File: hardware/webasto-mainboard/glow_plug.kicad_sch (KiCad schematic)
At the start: 23 parts, among them Q11 SSM3J374R, Q12 2N7002, Q13 SUD50P04-08, Q14 SUD50P04-08, Q15 SUD50P04-08, Q16 SUD50P04-08, Q17 SUD50P04-08, Q18 2N7002, Q19 2N7002, U6 LM7805_TO220, U7 INA219BxDCN

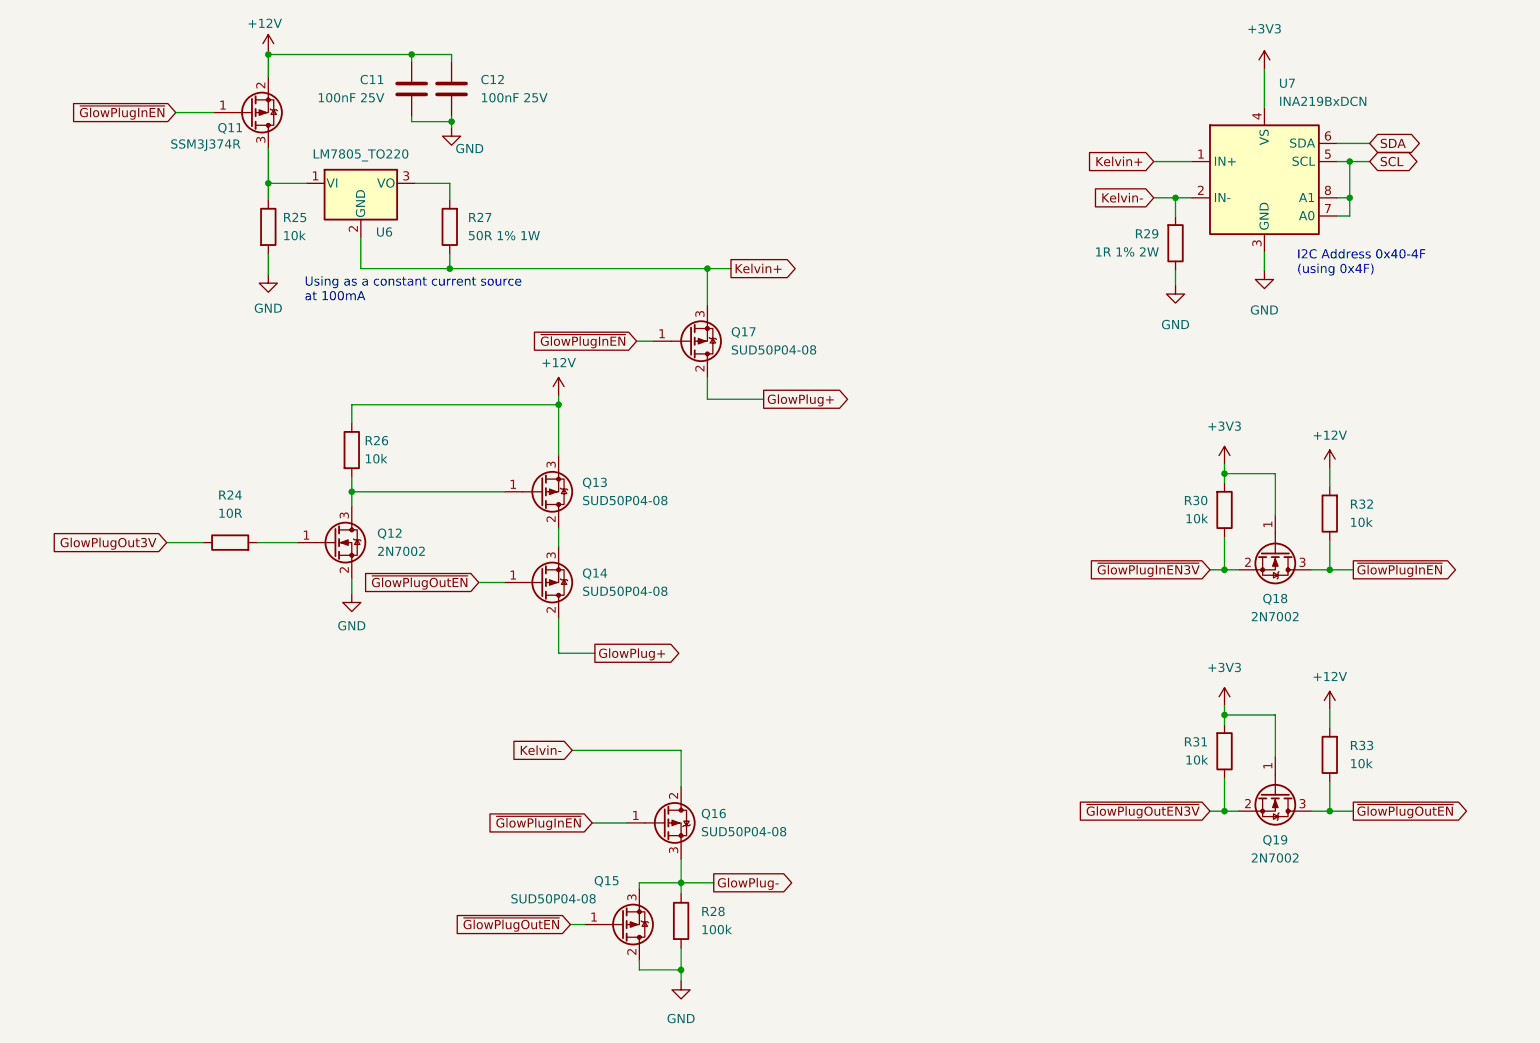
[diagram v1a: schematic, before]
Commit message: Added the LEDs onto the board and init
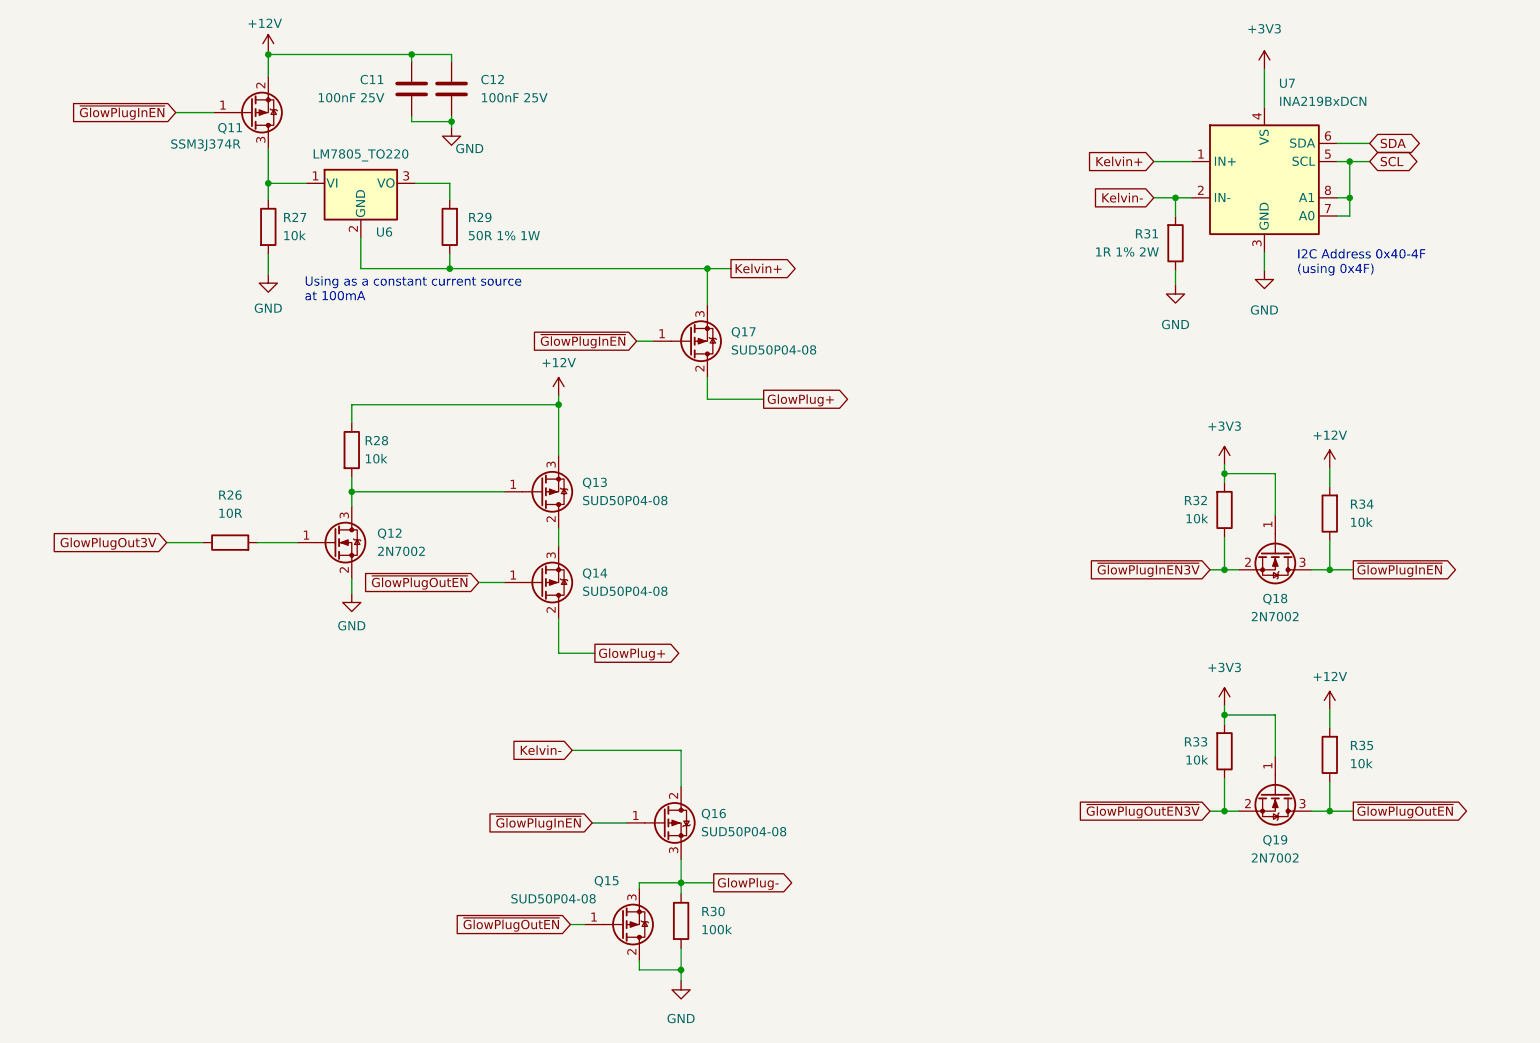
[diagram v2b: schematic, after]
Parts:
- renumbered R24 to R26, R25 to R27, R26 to R28, R27 to R29, R28 to R30, R29 to R31, R30 to R32, R31 to R33, R32 to R34, R33 to R35
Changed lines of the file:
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@@
   (symbol (lib_name "+3V3_1") (lib_id "power:+3V3") (at 202.565 29.972 0) (unit 1)
     (in_bom yes) (on_board yes) (fields_autoplaced)
-    (property "Reference" "#PWR063" (id 0) (at 202.565 33.782 0)
+    (property "Reference" "#PWR065" (id 0) (at 202.565 33.782 0)
       (effects (font (size 1.27 1.27)) hide)
     )
@@
   (symbol (lib_name "GND_8") (lib_id "power:GND") (at 202.565 58.166 0) (unit 1)
     (in_bom yes) (on_board yes) (fields_autoplaced)
-    (property "Reference" "#PWR064" (id 0) (at 202.565 64.516 0)
+    (property "Reference" "#PWR066" (id 0) (at 202.565 64.516 0)
       (effects (font (size 1.27 1.27)) hide)
     )
@@
   (symbol (lib_id "Device:R") (at 120.904 149.225 0) (unit 1)
     (in_bom yes) (on_board yes) (fields_autoplaced)
-    (property "Reference" "R28" (id 0) (at 123.698 147.9549 0)
+    (property "Reference" "R30" (id 0) (at 123.698 147.9549 0)
       (effects (font (size 1.27 1.27)) (justify left))
     )
@@
   (symbol (lib_id "Device:R") (at 74.803 83.312 0) (unit 1)
     (in_bom yes) (on_board yes) (fields_autoplaced)
-    (property "Reference" "R26" (id 0) (at 76.581 82.0419 0)
+    (property "Reference" "R28" (id 0) (at 76.581 82.0419 0)
       (effects (font (size 1.27 1.27)) (justify left))
     )
@@
   (symbol (lib_id "Device:R") (at 88.519 52.07 180) (unit 1)
     (in_bom yes) (on_board yes)
-    (property "Reference" "R27" (id 0) (at 91.059 50.7999 0)
+    (property "Reference" "R29" (id 0) (at 91.059 50.7999 0)
       (effects (font (size 1.27 1.27)) (justify right))
     )
@@
   (symbol (lib_name "+3V3_2") (lib_id "power:+3V3") (at 196.977 85.344 0) (unit 1)
     (in_bom yes) (on_board yes) (fields_autoplaced)
-    (property "Reference" "#PWR061" (id 0) (at 196.977 89.154 0)
+    (property "Reference" "#PWR063" (id 0) (at 196.977 89.154 0)
       (effects (font (size 1.27 1.27)) hide)
     )
@@
   (symbol (lib_name "GND_2") (lib_id "power:GND") (at 74.803 103.378 0) (unit 1)
     (in_bom yes) (on_board yes) (fields_autoplaced)
-    (property "Reference" "#PWR056" (id 0) (at 74.803 109.728 0)
+    (property "Reference" "#PWR058" (id 0) (at 74.803 109.728 0)
       (effects (font (size 1.27 1.27)) hide)
     )
@@
   (symbol (lib_id "Device:R") (at 63.119 52.07 0) (unit 1)
     (in_bom yes) (on_board yes)
-    (property "Reference" "R25" (id 0) (at 65.151 50.7999 0)
+    (property "Reference" "R27" (id 0) (at 65.151 50.7999 0)
       (effects (font (size 1.27 1.27)) (justify left))
     )
@@
   (symbol (lib_name "+3V3_2") (lib_id "power:+3V3") (at 196.977 119.126 0) (unit 1)
     (in_bom yes) (on_board yes) (fields_autoplaced)
-    (property "Reference" "#PWR062" (id 0) (at 196.977 122.936 0)
+    (property "Reference" "#PWR064" (id 0) (at 196.977 122.936 0)
       (effects (font (size 1.27 1.27)) hide)
     )
@@
   (symbol (lib_id "Device:R") (at 57.785 96.266 90) (unit 1)
     (in_bom yes) (on_board yes) (fields_autoplaced)
-    (property "Reference" "R24" (id 0) (at 57.785 89.662 90))
+    (property "Reference" "R26" (id 0) (at 57.785 89.662 90))
     (property "Value" "10R" (id 1) (at 57.785 92.202 90))
     (property "Footprint" "Resistor_SMD:R_0805_2012Metric_Pad1.20x1.40mm_HandSolder" (id 2) (at 57.785 98.044 90)
@@
   (symbol (lib_id "Device:R") (at 196.977 125.476 0) (mirror x) (unit 1)
     (in_bom yes) (on_board yes) (fields_autoplaced)
-    (property "Reference" "R31" (id 0) (at 194.691 124.2059 0)
+    (property "Reference" "R33" (id 0) (at 194.691 124.2059 0)
       (effects (font (size 1.27 1.27)) (justify right))
     )
@@
   (symbol (lib_name "GND_9") (lib_id "power:GND") (at 120.904 157.607 0) (unit 1)
     (in_bom yes) (on_board yes) (fields_autoplaced)
-    (property "Reference" "#PWR059" (id 0) (at 120.904 163.957 0)
+    (property "Reference" "#PWR061" (id 0) (at 120.904 163.957 0)
       (effects (font (size 1.27 1.27)) hide)
     )
@@
   (symbol (lib_name "+12V_3") (lib_id "power:+12V") (at 211.709 85.852 0) (unit 1)
     (in_bom yes) (on_board yes) (fields_autoplaced)
-    (property "Reference" "#PWR065" (id 0) (at 211.709 89.662 0)
+    (property "Reference" "#PWR067" (id 0) (at 211.709 89.662 0)
       (effects (font (size 1.27 1.27)) hide)
     )
@@
   (symbol (lib_name "GND_5") (lib_id "power:GND") (at 88.773 38.1 0) (unit 1)
     (in_bom yes) (on_board yes)
-    (property "Reference" "#PWR057" (id 0) (at 88.773 44.45 0)
+    (property "Reference" "#PWR059" (id 0) (at 88.773 44.45 0)
       (effects (font (size 1.27 1.27)) hide)
     )
@@
   (symbol (lib_id "Device:R") (at 211.709 92.202 180) (unit 1)
     (in_bom yes) (on_board yes) (fields_autoplaced)
-    (property "Reference" "R32" (id 0) (at 214.503 90.9319 0)
+    (property "Reference" "R34" (id 0) (at 214.503 90.9319 0)
       (effects (font (size 1.27 1.27)) (justify right))
     )
@@
   (symbol (lib_name "GND_8") (lib_id "power:GND") (at 190.119 60.198 0) (unit 1)
     (in_bom yes) (on_board yes) (fields_autoplaced)
-    (property "Reference" "#PWR060" (id 0) (at 190.119 66.548 0)
+    (property "Reference" "#PWR062" (id 0) (at 190.119 66.548 0)
       (effects (font (size 1.27 1.27)) hide)
     )
@@
   (symbol (lib_name "+12V_2") (lib_id "power:+12V") (at 63.119 27.686 0) (unit 1)
     (in_bom yes) (on_board yes)
-    (property "Reference" "#PWR054" (id 0) (at 63.119 31.496 0)
+    (property "Reference" "#PWR056" (id 0) (at 63.119 31.496 0)
       (effects (font (size 1.27 1.27)) hide)
     )
@@
   (symbol (lib_name "+12V_3") (lib_id "power:+12V") (at 211.709 119.634 0) (unit 1)
     (in_bom yes) (on_board yes) (fields_autoplaced)
-    (property "Reference" "#PWR066" (id 0) (at 211.709 123.444 0)
+    (property "Reference" "#PWR068" (id 0) (at 211.709 123.444 0)
       (effects (font (size 1.27 1.27)) hide)
     )
@@
   (symbol (lib_name "GND_3") (lib_id "power:GND") (at 63.119 58.674 0) (unit 1)
     (in_bom yes) (on_board yes) (fields_autoplaced)
-    (property "Reference" "#PWR055" (id 0) (at 63.119 65.024 0)
+    (property "Reference" "#PWR057" (id 0) (at 63.119 65.024 0)
       (effects (font (size 1.27 1.27)) hide)
     )
@@
   (symbol (lib_id "Device:R") (at 211.709 125.984 180) (unit 1)
     (in_bom yes) (on_board yes) (fields_autoplaced)
-    (property "Reference" "R33" (id 0) (at 214.503 124.7139 0)
+    (property "Reference" "R35" (id 0) (at 214.503 124.7139 0)
       (effects (font (size 1.27 1.27)) (justify right))
     )
@@
   (symbol (lib_id "Device:R") (at 190.119 54.356 0) (mirror x) (unit 1)
     (in_bom yes) (on_board yes) (fields_autoplaced)
-    (property "Reference" "R29" (id 0) (at 187.833 53.0859 0)
+    (property "Reference" "R31" (id 0) (at 187.833 53.0859 0)
       (effects (font (size 1.27 1.27)) (justify right))
     )
@@
   (symbol (lib_name "+12V_1") (lib_id "power:+12V") (at 103.759 75.692 0) (unit 1)
     (in_bom yes) (on_board yes) (fields_autoplaced)
-    (property "Reference" "#PWR058" (id 0) (at 103.759 79.502 0)
+    (property "Reference" "#PWR060" (id 0) (at 103.759 79.502 0)
       (effects (font (size 1.27 1.27)) hide)
     )
@@
   (symbol (lib_id "Device:R") (at 196.977 91.694 0) (mirror x) (unit 1)
     (in_bom yes) (on_board yes) (fields_autoplaced)
-    (property "Reference" "R30" (id 0) (at 194.691 90.4239 0)
-      (effects (font (size 1.27 1.27)) (justify right))
-    )
+    (property "Reference" "R32" (id 0) (at 194.691 90.4239 0)
+      (effects (font (size 1.27 1.27)) (justify right))
+    )
